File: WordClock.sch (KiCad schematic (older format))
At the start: 16 parts, among them J1 Conn_01x01, J2 Conn_01x01, J3 Conn_01x01, U1 LF120_TO220, U2 AP1117-50

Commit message: Started assigning footprints. Much cheaper to use the two channel n-fet for led driving. Need to change schematic to reflec.
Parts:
- C2, C4: value C -> 33uF; footprint (none) -> Capacitors_SMD:C_0805_HandSoldering
- C3, C5: value C -> 0.1uF; footprint (none) -> Capacitors_SMD:C_0805_HandSoldering
- D1, D2: footprint (none) -> LEDs:LED_0805_HandSoldering
- D3: footprint (none) -> Diodes_THT:Diode_Bridge_Round_D8.9mm
- R1, R2: value R -> 1K; footprint (none) -> Resistors_SMD:R_0603_HandSoldering
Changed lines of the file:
@@
 	1    0    0    -1
 $EndComp
-Wire Wire Line
-	1600 3600 1900 3600
-Wire Wire Line
-	1900 3600 1900 3750
-Wire Wire Line
-	1900 3200 1600 3200
-Wire Wire Line
-	1600 2850 1900 2850
 $Comp
 L PWR_FLAG #FLG02
@@
 	1    0    0    -1
 $EndComp
-Wire Wire Line
-	1250 1350 1250 1600
 $Comp
 L +5V #PWR05
@@
 	-1   0    0    1
 $EndComp
-Wire Wire Line
-	1750 1350 1750 1650
-Wire Notes Line
-	950  1000 2050 1000
-Wire Notes Line
-	2050 1000 2050 1900
-Wire Notes Line
-	2050 1900 950  1900
-Wire Notes Line
-	950  1900 950  1000
 Text Notes 950  950  0    60   ~ 0
 POWER FLAGS
-Wire Notes Line
-	1000 2500 2400 2500
-Wire Notes Line
-	2400 2500 2400 4300
-Wire Notes Line
-	2400 4300 1000 4300
-Wire Notes Line
-	1000 4300 1000 2500
 Text Notes 1000 2400 0    60   ~ 0
 POWER CONNECTORS
@@
 F 0 "D3" H 5050 2225 50  0000 L CNN
 F 1 "D_Bridge_+A-A" H 5050 2150 50  0000 L CNN
-F 2 "" H 5000 1950 50  0001 C CNN
+F 2 "Diodes_THT:Diode_Bridge_Round_D8.9mm" H 5000 1950 50  0001 C CNN
 F 3 "" H 5000 1950 50  0001 C CNN
 	1    5000 1950
@@
 P 6500 2200
 F 0 "C2" H 6525 2300 50  0000 L CNN
-F 1 "C" H 6525 2100 50  0000 L CNN
-F 2 "" H 6538 2050 50  0001 C CNN
+F 1 "33uF" H 6525 2100 50  0000 L CNN
+F 2 "Capacitors_SMD:C_0805_HandSoldering" H 6538 2050 50  0001 C CNN
 F 3 "" H 6500 2200 50  0001 C CNN
 	1    6500 2200
@@
 	0    1    1    0
 $EndComp
-Wire Wire Line
-	3650 1600 4100 1600
-Wire Wire Line
-	4400 1600 5000 1600
-Wire Wire Line
-	5000 1600 5000 1650
-Wire Wire Line
-	3650 2350 5000 2350
-Wire Wire Line
-	5000 2350 5000 2250
-Wire Wire Line
-	5300 1950 6750 1950
-Wire Wire Line
-	6050 1950 6050 2050
 $Comp
 L GND #PWR06
@@
 	1    0    0    -1
 $EndComp
-Wire Wire Line
-	6050 2350 6050 2500
 $Comp
 L GND #PWR07
@@
 	1    0    0    -1
 $EndComp
-Wire Wire Line
-	4500 2050 4500 1950
-Wire Wire Line
-	4500 1950 4700 1950
 $Comp
 L LF120_TO220 U1
@@
 P 7600 2200
 F 0 "C3" H 7625 2300 50  0000 L CNN
-F 1 "C" H 7625 2100 50  0000 L CNN
-F 2 "" H 7638 2050 50  0001 C CNN
+F 1 "0.1uF" H 7625 2100 50  0000 L CNN
+F 2 "Capacitors_SMD:C_0805_HandSoldering" H 7638 2050 50  0001 C CNN
 F 3 "" H 7600 2200 50  0001 C CNN
 	1    7600 2200
 	1    0    0    -1
 $EndComp
-Connection ~ 6050 1950
-Wire Wire Line
-	6500 2050 6500 1950
-Connection ~ 6500 1950
 $Comp
 L GND #PWR08
@@
 	1    0    0    -1
 $EndComp
-Wire Wire Line
-	6500 2500 6500 2350
-Wire Wire Line
-	7350 1950 8200 1950
-Wire Wire Line
-	7600 1950 7600 2050
 $Comp
 L GND #PWR09
@@
 	1    0    0    -1
 $EndComp
-Wire Wire Line
-	7600 2500 7600 2350
-Wire Wire Line
-	7050 2250 7050 2500
 $Comp
 L AP1117-50 U2
@@
 P 8000 2200
 F 0 "C4" H 8025 2300 50  0000 L CNN
-F 1 "C" H 8025 2100 50  0000 L CNN
-F 2 "" H 8038 2050 50  0001 C CNN
+F 1 "33uF" H 8025 2100 50  0000 L CNN
+F 2 "Capacitors_SMD:C_0805_HandSoldering" H 8038 2050 50  0001 C CNN
 F 3 "" H 8000 2200 50  0001 C CNN
 	1    8000 2200
@@
 P 9050 2200
 F 0 "C5" H 9075 2300 50  0000 L CNN
-F 1 "C" H 9075 2100 50  0000 L CNN
-F 2 "" H 9088 2050 50  0001 C CNN
+F 1 "0.1uF" H 9075 2100 50  0000 L CNN
+F 2 "Capacitors_SMD:C_0805_HandSoldering" H 9088 2050 50  0001 C CNN
 F 3 "" H 9050 2200 50  0001 C CNN
 	1    9050 2200
 	1    0    0    -1
 $EndComp
-Wire Wire Line
-	8800 1950 9200 1950
-Wire Wire Line
-	9200 1950 9200 1700
 $Comp
 L GND #PWR013
@@
 	1    0    0    -1
 $EndComp
-Wire Wire Line
-	8500 2250 8500 2500
-Wire Wire Line
-	9050 2050 9050 1950
-Connection ~ 9050 1950
-Wire Wire Line
-	9050 2350 9050 2500
-Connection ~ 7600 1950
-Wire Wire Line
-	8000 2050 8000 1950
-Connection ~ 8000 1950
-Wire Wire Line
-	8000 2500 8000 2350
 $Comp
 L +12V #PWR015
@@
 	1    0    0    -1
 $EndComp
-Wire Wire Line
-	7850 1850 7850 1950
-Connection ~ 7850 1950
 $Comp
 L LED D1
@@
 F 0 "D1" H 3650 3850 50  0000 C CNN
 F 1 "LED" H 3650 3650 50  0000 C CNN
-F 2 "" H 3650 3750 50  0001 C CNN
+F 2 "LEDs:LED_0805_HandSoldering" H 3650 3750 50  0001 C CNN
 F 3 "" H 3650 3750 50  0001 C CNN
 	1    3650 3750
@@
 F 0 "D2" H 4000 3850 50  0000 C CNN
 F 1 "LED" H 4000 3650 50  0000 C CNN
-F 2 "" H 4000 3750 50  0001 C CNN
+F 2 "LEDs:LED_0805_HandSoldering" H 4000 3750 50  0001 C CNN
 F 3 "" H 4000 3750 50  0001 C CNN
 	1    4000 3750
@@
 P 3650 3350
 F 0 "R1" V 3730 3350 50  0000 C CNN
-F 1 "R" V 3650 3350 50  0000 C CNN
-F 2 "" V 3580 3350 50  0001 C CNN
+F 1 "1K" V 3650 3350 50  0000 C CNN
+F 2 "Resistors_SMD:R_0603_HandSoldering" V 3580 3350 50  0001 C CNN
 F 3 "" H 3650 3350 50  0001 C CNN
 	1    3650 3350
@@
 P 4000 3350
 F 0 "R2" V 4080 3350 50  0000 C CNN
-F 1 "R" V 4000 3350 50  0000 C CNN
-F 2 "" V 3930 3350 50  0001 C CNN
+F 1 "1K" V 4000 3350 50  0000 C CNN
+F 2 "Resistors_SMD:R_0603_HandSoldering" V 3930 3350 50  0001 C CNN
 F 3 "" H 4000 3350 50  0001 C CNN
 	1    4000 3350
 	1    0    0    -1
 $EndComp
-Wire Wire Line
-	3650 3500 3650 3600
-Wire Wire Line
-	3650 3900 3650 4000
-Wire Wire Line
-	4000 3900 4000 4000
-Wire Wire Line
-	4000 3500 4000 3600
-Wire Wire Line
-	3650 3100 3650 3200
-Wire Wire Line
-	4000 3100 4000 3200
-Wire Notes Line
-	3100 1250 3100 4300
-Wire Notes Line
-	3100 4300 9500 4300
-Wire Notes Line
-	9500 4300 9500 1250
-Wire Notes Line
-	9500 1250 3100 1250
 Text Notes 3100 1200 0    60   ~ 0
 POWER SUPPLY
@@
 	1    0    0    -1
 $EndComp
-Wire Wire Line
-	5225 5850 5400 5850
-Wire Wire Line
-	5400 5850 5400 5975
 $Comp
 L +12V #PWR021
@@
 $EndComp
 Wire Wire Line
+	1600 3600 1900 3600
+Wire Wire Line
+	1900 3600 1900 3750
+Wire Wire Line
+	1900 3200 1600 3200
+Wire Wire Line
+	1600 2850 1900 2850
+Wire Wire Line
+	1250 1350 1250 1600
+Wire Wire Line
+	1750 1350 1750 1650
+Wire Notes Line
+	950  1000 2050 1000
+Wire Notes Line
+	2050 1000 2050 1900
+Wire Notes Line
+	2050 1900 950  1900
+Wire Notes Line
+	950  1900 950  1000
+Wire Notes Line
+	1000 2500 2400 2500
+Wire Notes Line
+	2400 2500 2400 4300
+Wire Notes Line
+	2400 4300 1000 4300
+Wire Notes Line
+	1000 4300 1000 2500
+Wire Wire Line
+	3650 1600 4100 1600
+Wire Wire Line
+	4400 1600 5000 1600
+Wire Wire Line
+	5000 1600 5000 1650
+Wire Wire Line
+	3650 2350 5000 2350
+Wire Wire Line
+	5000 2350 5000 2250
+Wire Wire Line
+	6050 1950 6050 2050
+Wire Wire Line
+	6050 2350 6050 2500
+Wire Wire Line
+	4500 2050 4500 1950
+Wire Wire Line
+	4500 1950 4700 1950
+Connection ~ 6050 1950
+Wire Wire Line
+	6500 2050 6500 1950
+Connection ~ 6500 1950
+Wire Wire Line
+	6500 2500 6500 2350
+Wire Wire Line
+	7350 1950 8200 1950
+Wire Wire Line
+	7600 1950 7600 2050
+Wire Wire Line
+	7600 2500 7600 2350
+Wire Wire Line
+	7050 2250 7050 2500
+Wire Wire Line
+	8800 1950 9200 1950
+Wire Wire Line
+	9200 1950 9200 1700
+Wire Wire Line
+	8500 2250 8500 2500
+Wire Wire Line
+	9050 2050 9050 1950
+Connection ~ 9050 1950
+Wire Wire Line
+	9050 2350 9050 2500
+Connection ~ 7600 1950
+Wire Wire Line
+	8000 2050 8000 1950
+Connection ~ 8000 1950
+Wire Wire Line
+	8000 2500 8000 2350
+Wire Wire Line
+	7850 1850 7850 1950
+Connection ~ 7850 1950
+Wire Wire Line
+	3650 3500 3650 3600
+Wire Wire Line
+	3650 3900 3650 4000
+Wire Wire Line
+	4000 3900 4000 4000
+Wire Wire Line
+	4000 3500 4000 3600
+Wire Wire Line
+	3650 3100 3650 3200
+Wire Wire Line
+	4000 3100 4000 3200
+Wire Notes Line
+	3100 1250 3100 4300
+Wire Notes Line
+	3100 4300 9500 4300
+Wire Notes Line
+	9500 4300 9500 1250
+Wire Notes Line
+	9500 1250 3100 1250
+Wire Wire Line
+	5225 5850 5400 5850
+Wire Wire Line
+	5400 5850 5400 5975
+Wire Wire Line
 	5225 5125 5400 5125
 Wire Wire Line
@@
 Wire Wire Line
 	5525 5475 5225 5475
+Wire Wire Line
+	5300 1950 6750 1950
 $EndSCHEMATC

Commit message: Finished component footprint assignments and began rough layout of components.
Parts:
- C1: value C -> 1000uF; footprint (none) -> Capacitors_THT:CP_Radial_D18.0mm_P7.50mm
- F1: footprint (none) -> Fuse_Holders_and_Fuses:Fuse_SMD1206_HandSoldering
- J1, J2, J3: footprint (none) -> Wire_Pads:SolderWirePad_single_SMD_5x10mm
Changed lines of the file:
@@
 LIBS:contrib
 LIBS:valves
+LIBS:NUD3124
 LIBS:WordClock-cache
 EELAYER 25 0
@@
 F 0 "J1" H 1400 2950 50  0000 C CNN
 F 1 "Conn_01x01" H 1400 2750 50  0000 C CNN
-F 2 "" H 1400 2850 50  0001 C CNN
+F 2 "Wire_Pads:SolderWirePad_single_SMD_5x10mm" H 1400 2850 50  0001 C CNN
 F 3 "" H 1400 2850 50  0001 C CNN
 	1    1400 2850
@@
 F 0 "J2" H 1400 3300 50  0000 C CNN
 F 1 "Conn_01x01" H 1400 3100 50  0000 C CNN
-F 2 "" H 1400 3200 50  0001 C CNN
+F 2 "Wire_Pads:SolderWirePad_single_SMD_5x10mm" H 1400 3200 50  0001 C CNN
 F 3 "" H 1400 3200 50  0001 C CNN
 	1    1400 3200
@@
 F 0 "J3" H 1400 3700 50  0000 C CNN
 F 1 "Conn_01x01" H 1400 3500 50  0000 C CNN
-F 2 "" H 1400 3600 50  0001 C CNN
+F 2 "Wire_Pads:SolderWirePad_single_SMD_5x10mm" H 1400 3600 50  0001 C CNN
 F 3 "" H 1400 3600 50  0001 C CNN
 	1    1400 3600
@@
 P 6050 2200
 F 0 "C1" H 6075 2300 50  0000 L CNN
-F 1 "C" H 6075 2100 50  0000 L CNN
-F 2 "" H 6088 2050 50  0001 C CNN
+F 1 "1000uF" H 6075 2100 50  0000 L CNN
+F 2 "Capacitors_THT:CP_Radial_D18.0mm_P7.50mm" H 6088 2050 50  0001 C CNN
 F 3 "" H 6050 2200 50  0001 C CNN
 	1    6050 2200
@@
 F 0 "F1" V 4330 1600 50  0000 C CNN
 F 1 "Fuse" V 4150 1600 50  0000 C CNN
-F 2 "" V 4180 1600 50  0001 C CNN
+F 2 "Fuse_Holders_and_Fuses:Fuse_SMD1206_HandSoldering" V 4180 1600 50  0001 C CNN
 F 3 "" H 4250 1600 50  0001 C CNN
 	1    4250 1600

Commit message: Routed power, clock, switches and started on arduino/IO expanders
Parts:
- removed U1: LF120_TO220, TO_SOT_Packages_THT:TO-220_Vertical, symbol LF120_TO220
- added U1: AP1117-50, TO_SOT_Packages_SMD:SOT-223-3_TabPin2, symbol AP1117-50
- C2: value 33uF -> 10uF
- C3: value 0.1uF -> 10uF
- C4: value 33uF -> 4.7uF
- C5: value 0.1uF -> 4.7uF
- U2: footprint TO_SOT_Packages_SMD:SOT-223-3Lead_TabPin2 -> TO_SOT_Packages_SMD:SOT-223-3_TabPin2
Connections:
- net labels added: AC-
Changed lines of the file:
@@
 AC+
 Text GLabel 1900 3200 2    60   Input ~ 0
-AC+
+AC-
 $Comp
 L GND #PWR01
@@
 AC+
 Text GLabel 3650 2350 0    60   Input ~ 0
-AC+
+AC-
 $Comp
 L D_Bridge_+A-A D3
@@
 P 6500 2200
 F 0 "C2" H 6525 2300 50  0000 L CNN
-F 1 "33uF" H 6525 2100 50  0000 L CNN
+F 1 "10uF" H 6525 2100 50  0000 L CNN
 F 2 "Capacitors_SMD:C_0805_HandSoldering" H 6538 2050 50  0001 C CNN
 F 3 "" H 6500 2200 50  0001 C CNN
@@
 $EndComp
 $Comp
-L LF120_TO220 U1
-U 1 1 59E449DA
-P 7050 1950
-F 0 "U1" H 6900 2075 50  0000 C CNN
-F 1 "LF120_TO220" H 7050 2075 50  0000 L CNN
-F 2 "TO_SOT_Packages_THT:TO-220_Vertical" H 7050 2175 50  0001 C CIN
-F 3 "" H 7050 1900 50  0001 C CNN
-	1    7050 1950
-	1    0    0    -1
-$EndComp
-$Comp
 L C C3
 U 1 1 59E44A85
 P 7600 2200
 F 0 "C3" H 7625 2300 50  0000 L CNN
-F 1 "0.1uF" H 7625 2100 50  0000 L CNN
+F 1 "10uF" H 7625 2100 50  0000 L CNN
 F 2 "Capacitors_SMD:C_0805_HandSoldering" H 7638 2050 50  0001 C CNN
 F 3 "" H 7600 2200 50  0001 C CNN
@@
 F 0 "U2" H 8350 2075 50  0000 C CNN
 F 1 "AP1117-50" H 8500 2075 50  0000 L CNN
-F 2 "TO_SOT_Packages_SMD:SOT-223-3Lead_TabPin2" H 8500 2150 50  0001 C CNN
+F 2 "TO_SOT_Packages_SMD:SOT-223-3_TabPin2" H 8500 2150 50  0001 C CNN
 F 3 "" H 8600 1700 50  0001 C CNN
 	1    8500 1950
@@
 P 8000 2200
 F 0 "C4" H 8025 2300 50  0000 L CNN
-F 1 "33uF" H 8025 2100 50  0000 L CNN
+F 1 "4.7uF" H 8025 2100 50  0000 L CNN
 F 2 "Capacitors_SMD:C_0805_HandSoldering" H 8038 2050 50  0001 C CNN
 F 3 "" H 8000 2200 50  0001 C CNN
@@
 P 9050 2200
 F 0 "C5" H 9075 2300 50  0000 L CNN
-F 1 "0.1uF" H 9075 2100 50  0000 L CNN
+F 1 "4.7uF" H 9075 2100 50  0000 L CNN
 F 2 "Capacitors_SMD:C_0805_HandSoldering" H 9088 2050 50  0001 C CNN
 F 3 "" H 9050 2200 50  0001 C CNN
@@
 Wire Wire Line
 	5300 1950 6750 1950
+$Comp
+L AP1117-50 U1
+U 1 1 59F6A644
+P 7050 1950
+F 0 "U1" H 6900 2075 50  0000 C CNN
+F 1 "AP1117-50" H 7050 2075 50  0000 L CNN
+F 2 "TO_SOT_Packages_SMD:SOT-223-3_TabPin2" H 7050 2150 50  0001 C CNN
+F 3 "" H 7150 1700 50  0001 C CNN
+	1    7050 1950
+	1    0    0    -1
+$EndComp
 $EndSCHEMATC

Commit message: Started placing and routing new board with updated schematic. Requries RTC.
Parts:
- removed C1: 1000uF, Capacitors_THT:CP_Radial_D18.0mm_P7.50mm, symbol C
- removed C2, C3: 10uF, Capacitors_SMD:C_0805_HandSoldering, symbol C
- removed D3: D_Bridge_+A-A, Diodes_THT:Diode_Bridge_Round_D8.9mm, symbol D_Bridge_+A-A
- removed F1: Fuse, Fuse_Holders_and_Fuses:Fuse_SMD1206_HandSoldering, symbol Fuse
- removed J1, J2, J3: Conn_01x01, Wire_Pads:SolderWirePad_single_SMD_5x10mm, symbol Conn_01x01
- removed U1: AP1117-50, TO_SOT_Packages_SMD:SOT-223-3_TabPin2, symbol AP1117-50
- added J1: Conn_01x02, Connectors_Phoenix:PhoenixContact_MC-GF_02x3.50mm_Angled_ThreadedFlange, symbol Conn_01x02
- renumbered C4 to C1, C5 to C2, U2 to U1
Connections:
- net labels removed: AC+, AC-
- wire segments 42 -> 22
- no-connect marks 0 -> 1
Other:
- note removed: "POWER CONNECTORS"
- note removed: "POWER SUPPLY"
- moved on the sheet: C1, C2, D1, D2, R1, R2, U1

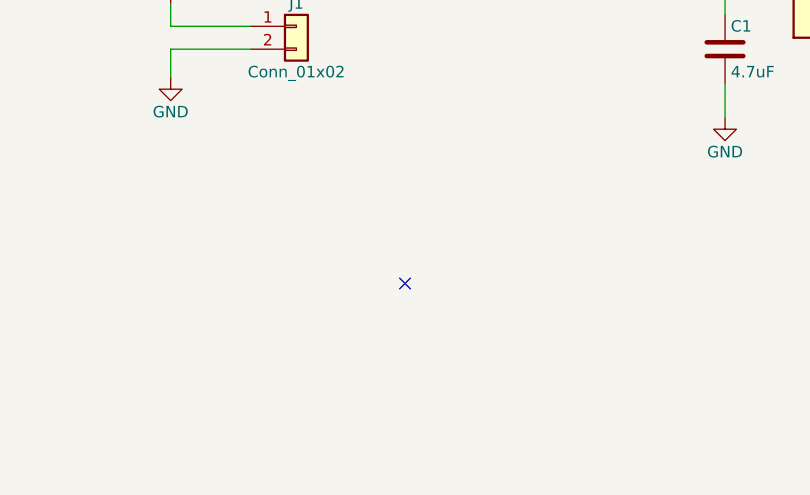
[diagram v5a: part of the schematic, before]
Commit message: Fabriation files from first board spin. Footpring for IO expander incorrect, wide version used now, began board routing with new footprints.
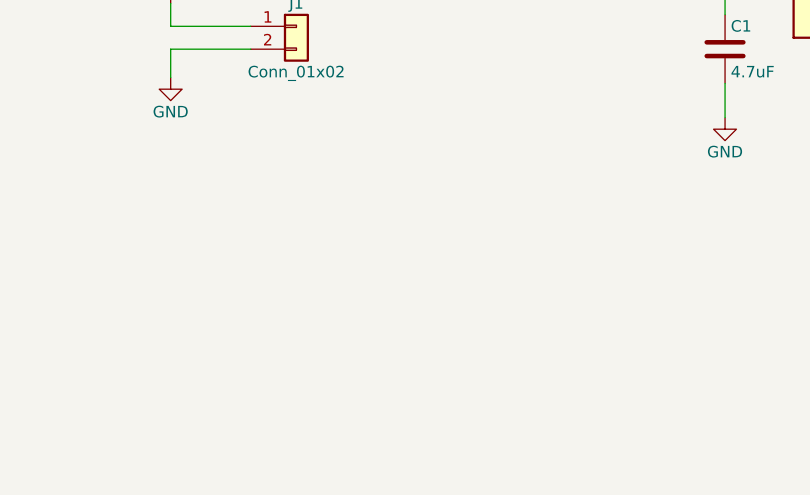
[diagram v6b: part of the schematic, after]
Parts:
- J1: footprint Connectors_Phoenix:PhoenixContact_MC-GF_02x3.50mm_Angled_ThreadedFlange -> Connectors_Phoenix:PhoenixContact_MC-G_02x3.50mm_Angled
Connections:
- no-connect marks 1 -> 0
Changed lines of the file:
@@
 LIBS:NUD3124
 LIBS:e2c-12nu
+LIBS:tiny_rtc
 LIBS:WordClock-cache
 EELAYER 25 0
@@
 F 0 "J1" H 4775 3875 50  0000 C CNN
 F 1 "Conn_01x02" H 4775 3575 50  0000 C CNN
-F 2 "Connectors_Phoenix:PhoenixContact_MC-GF_02x3.50mm_Angled_ThreadedFlange" H 4775 3775 50  0001 C CNN
+F 2 "Connectors_Phoenix:PhoenixContact_MC-G_02x3.50mm_Angled" H 4775 3775 50  0001 C CNN
 F 3 "" H 4775 3775 50  0001 C CNN
 	1    4775 3775
@@
 	-1   0    0    1
 $EndComp
-NoConn ~ 5250 4900
 $EndSCHEMATC
